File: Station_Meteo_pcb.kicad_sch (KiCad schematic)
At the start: 0 parts

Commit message: t
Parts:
- added U1: 4001, symbol 4xxx:4001

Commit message: test
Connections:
- net at U1.9: now also U1.6
- net at U1.5: now also U1.3
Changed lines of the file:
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@@
 	(generator_version "9.0")
 	(paper "A4")
+	(wire
+		(pts
+			(xy 107.95 116.84) (xy 191.77 116.84)
+		)
+		(stroke
+			(width 0)
+			(type default)
+		)
+	)
+	(wire
+		(pts
+			(xy 191.77 107.95) (xy 191.77 116.84)
+		)
+		(stroke
+			(width 0)
+			(type default)
+		)
+	)
+	(wire
+		(pts
+			(xy 107.95 101.6) (xy 107.95 116.84)
+		)
+		(stroke
+			(width 0)
+			(type default)
+		)
+	)
+	(wire
+		(pts
+			(xy 67.31 90.17) (xy 107.95 90.17)
+		)
+		(stroke
+			(width 0)
+			(type default)
+		)
+	)
+	(wire
+		(pts
+			(xy 107.95 90.17) (xy 107.95 96.52)
+		)
+		(stroke
+			(width 0)
+			(type default)
+		)
+	)
 	(symbol
 		(lib_id "4xxx:4001")

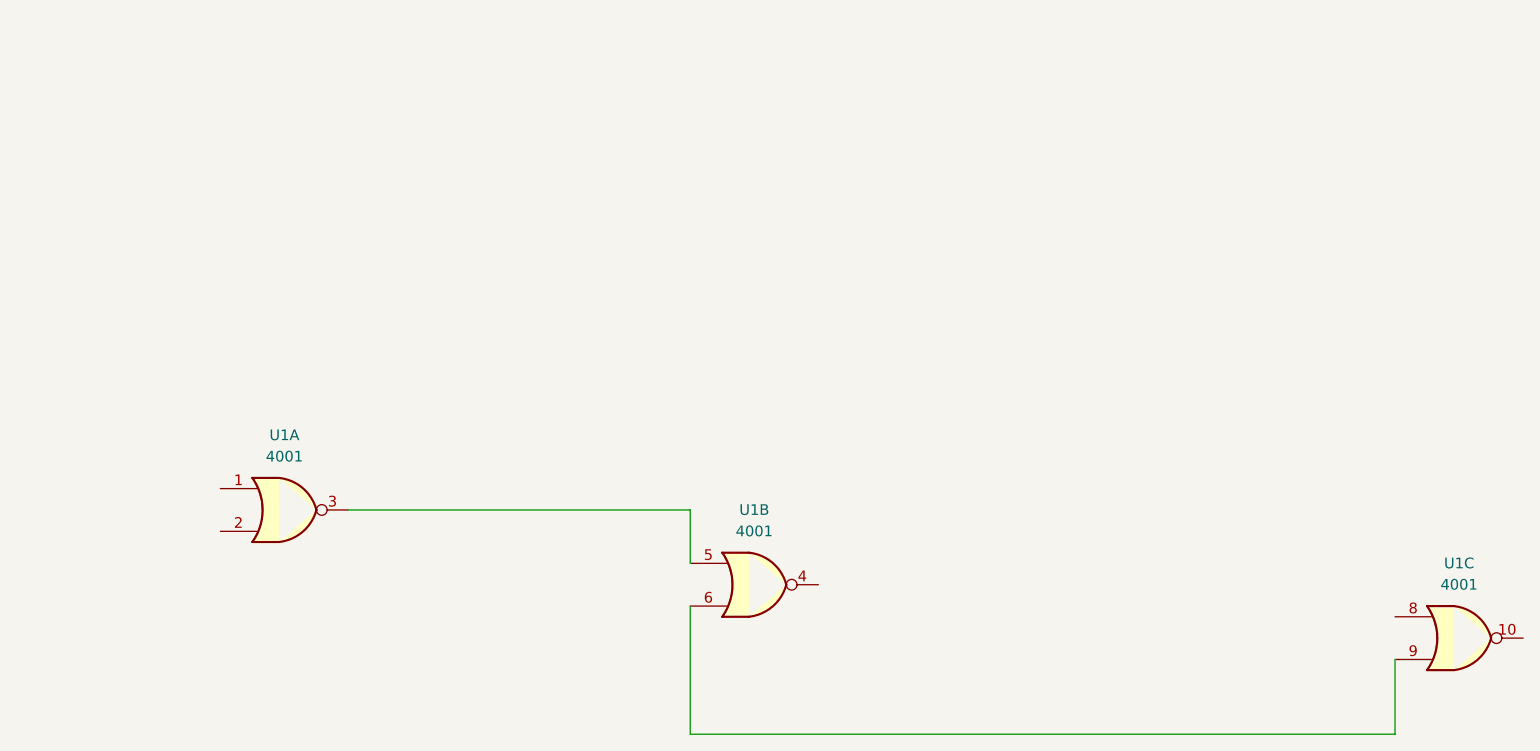
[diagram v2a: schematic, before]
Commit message: Schematique Capteurs
Mise en forme des pages pour les différents schémas kicad
Pages capteurs mais à vérifier
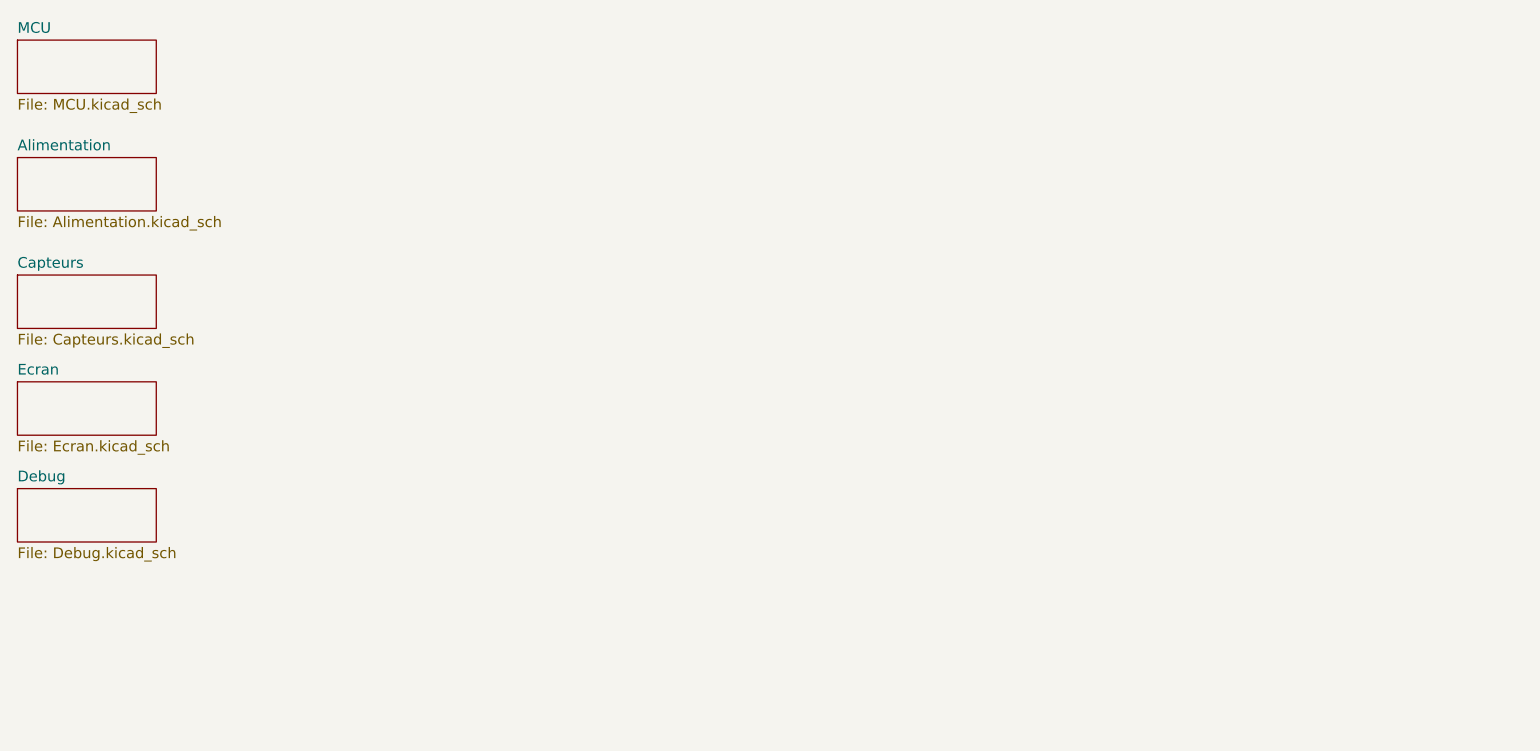
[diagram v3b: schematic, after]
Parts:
- removed U1: 4001, symbol 4xxx:4001
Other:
- added sheet Alimentation (Alimentation.kicad_sch)
- added sheet Capteurs (Capteurs.kicad_sch)
- added sheet Debug (Debug.kicad_sch)
- added sheet Ecran (Ecran.kicad_sch)
- added sheet MCU (MCU.kicad_sch)

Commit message: premieres modif depuis la review
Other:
- added sheet Connecteurs (Connecteurs.kicad_sch)
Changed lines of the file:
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@@
+	)
+	(sheet
+		(at 27.94 100.33)
+		(size 16.51 6.35)
+		(exclude_from_sim no)
+		(in_bom yes)
+		(on_board yes)
+		(dnp no)
+		(fields_autoplaced yes)
+		(stroke
+			(width 0.1524)
+			(type solid)
+		)
+		(fill
+			(color 0 0 0 0.0000)
+		)
+		(property "Sheetname" "Connecteurs"
+			(at 27.94 99.6184 0)
+			(effects
+				(font
+					(size 1.27 1.27)
+				)
+				(justify left bottom)
+			)
+		)
+		(property "Sheetfile" "Connecteurs.kicad_sch"
+			(at 27.94 107.2646 0)
+			(effects
+				(font
+					(size 1.27 1.27)
+				)
+				(justify left top)
+			)
+		)
+		(instances
+			(project "Station_Meteo_pcb"
+				(path "/90bd0b60-6e70-43e1-8410-99fb54688c17"
+					(page "7")
+				)
+			)
+		)
 	)
 	(sheet

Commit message: t
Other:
- removed sheet Debug
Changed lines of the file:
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@@
-	)
-	(sheet
-		(at 27.94 87.63)
-		(size 16.51 6.35)
-		(exclude_from_sim no)
-		(in_bom yes)
-		(on_board yes)
-		(dnp no)
-		(fields_autoplaced yes)
-		(stroke
-			(width 0.1524)
-			(type solid)
-		)
-		(fill
-			(color 0 0 0 0.0000)
-		)
-		(property "Sheetname" "Debug"
-			(at 27.94 86.9184 0)
-			(effects
-				(font
-					(size 1.27 1.27)
-				)
-				(justify left bottom)
-			)
-		)
-		(property "Sheetfile" "Debug.kicad_sch"
-			(at 27.94 94.5646 0)
-			(effects
-				(font
-					(size 1.27 1.27)
-				)
-				(justify left top)
-			)
-		)
-		(instances
-			(project "Station_Meteo_pcb"
-				(path "/90bd0b60-6e70-43e1-8410-99fb54688c17"
-					(page "6")
-				)
-			)
-		)
 	)
 	(sheet
@@
 	)
 	(sheet
-		(at 27.94 100.33)
+		(at 27.94 88.9)
 		(size 16.51 6.35)
 		(exclude_from_sim no)
@@
 		)
 		(property "Sheetname" "Connecteurs"
-			(at 27.94 99.6184 0)
+			(at 27.94 88.1884 0)
 			(effects
 				(font
@@
 		)
 		(property "Sheetfile" "Connecteurs.kicad_sch"
-			(at 27.94 107.2646 0)
+			(at 27.94 95.8346 0)
 			(effects
 				(font
